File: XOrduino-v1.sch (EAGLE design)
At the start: 56 parts, among them J1 USB MICRO, J2 8x1F-H8.5, J3 8x1F-H8.5, J4 6x1F-H8.5, U1 ATMEGA32U4-XUAU, U10 SLIDER, U3 2.5mm, U4 2.5mm, U5 2.5mm, U6 2.5mm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

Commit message: Attempt to route the board.  90% routed; may need to go to 4 layer board.
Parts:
- removed JP1: 10x1F-H8.5, SmartPrj:PINHD-1X10
- J1: value USB MICRO -> 10x1F-H8.5; device SmartPrj:MYCON2_USB-MINI-B -> SmartPrj:PINHD-1X10
- JP6: value (none) -> Sensor Routing
- L, ON, RX, TX: device led:LED5MM -> led:LED3MM
- S1: value (none) -> RESET
- S2: value 12mm Button -> 6mm Button; device SparkFun:SWITCH-MOMENTARY-212MM -> SparkFun-Electromechanical:TAC_SWITCHPTH
- U10: value SLIDER -> 10k; device SparkFun:SLIDER -> SparkFun-Electromechanical:POT
- renumbered U3 to J5, U4 to J6, U5 to J7, U6 to J8
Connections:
- removed net USBID: J1.ID
- net +5V: now also RN4D.2; no longer RN4C.2
- net A0: now also JP6-1.1; no longer JP6-1.2
- net A1: now also JP6-2.1; no longer JP6-2.2
- net A2: now also JP6-3.1; no longer JP6-3.2
- net A3: now also JP6-4.1; no longer JP6-4.2
- net A4: now also JP6-5.1; no longer JP6-5.2
- net A5: now also JP6-6.1; no longer JP6-6.2
- net AREF: now also J1.8; no longer JP1.8
- net D+: no longer J1.D+
- net D-: no longer J1.D-
- net D2/SDA: now also J1.9; no longer JP1.9
- net D3/SCL: now also J1.10; no longer JP1.10
- net D4: now also JP6-7.1; no longer JP6-7.2
- net GND: now also J1.7, S2.4; no longer J1.SH1, J1.SH2, J1.SH3, J1.SH4, J1.SH5, J1.SH6, JP1.7, S1.3, S2.2
- net IO10*: now also J1.3; no longer JP1.3
- net IO11*: now also J1.4; no longer JP1.4
- net IO12: now also J1.5; no longer JP1.5
- net IO13*: now also J1.6; no longer JP1.6
- net IO8: now also J1.1; no longer JP1.1
- net IO9*: now also J1.2; no longer JP1.2
- net LIGHT: now also JP6-6.2; no longer JP6-6.1
- net N$1: now also RN4B.1; no longer RN4A.1
- net N$2: now also RN4C.1; no longer RN4D.1
- net N$3: now also RN4D.1; no longer RN4C.1
- net N$4: now also RN4A.1; no longer RN4B.1
- net N$6: now also RN4C.2; no longer RN4D.2
- net RA: now also JP6-1.2; no longer JP6-1.1
- net RB: now also JP6-2.2; no longer JP6-2.1
- net RC: now also JP6-3.2; no longer JP6-3.1
- net RD: now also JP6-4.2; no longer JP6-4.1
- net RESET: no longer S1.2
- net SLIDER: now also JP6-7.2; no longer JP6-7.1
- net SOUND: now also JP6-5.2; no longer JP6-5.1
- net UGND: no longer J1.GND
- net XUSB: no longer J1.VBUS
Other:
- moved on the sheet: JP6-1, JP6-2, JP6-3, JP6-4, JP6-5, JP6-6, JP6-7, RN4

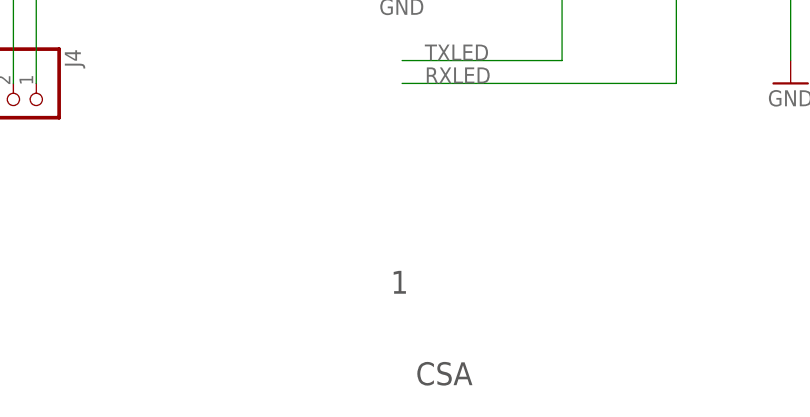
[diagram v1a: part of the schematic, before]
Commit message: XOrduino v2 -- move USB plug up a bit to allow XOstick to fit underneath.
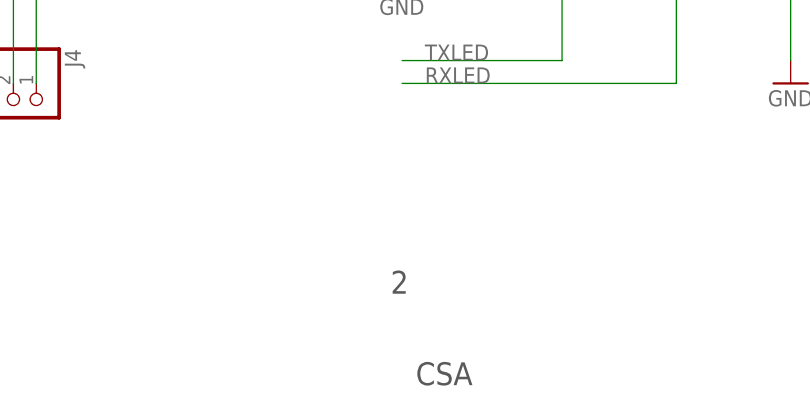
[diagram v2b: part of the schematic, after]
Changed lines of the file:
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@@
 <grid distance="0.1" unitdist="inch" unit="inch" style="lines" multiple="1" display="no" altdistance="0.01" altunitdist="inch" altunit="inch"/>
 <layers>
-<layer number="1" name="Top" color="4" fill="1" visible="yes" active="no"/>
-<layer number="2" name="Route2" color="1" fill="3" visible="yes" active="no"/>
-<layer number="3" name="Route3" color="4" fill="3" visible="yes" active="no"/>
-<layer number="4" name="Route4" color="1" fill="4" visible="yes" active="no"/>
-<layer number="5" name="Route5" color="4" fill="4" visible="yes" active="no"/>
-<layer number="6" name="Route6" color="1" fill="8" visible="yes" active="no"/>
-<layer number="7" name="Route7" color="4" fill="8" visible="yes" active="no"/>
-<layer number="8" name="Route8" color="1" fill="2" visible="yes" active="no"/>
-<layer number="9" name="Route9" color="4" fill="2" visible="yes" active="no"/>
-<layer number="10" name="Route10" color="1" fill="7" visible="yes" active="no"/>
-<layer number="11" name="Route11" color="4" fill="7" visible="yes" active="no"/>
-<layer number="12" name="Route12" color="1" fill="5" visible="yes" active="no"/>
-<layer number="13" name="Route13" color="4" fill="5" visible="yes" active="no"/>
-<layer number="14" name="Route14" color="1" fill="6" visible="yes" active="no"/>
-<layer number="15" name="Route15" color="4" fill="6" visible="yes" active="no"/>
-<layer number="16" name="Bottom" color="1" fill="1" visible="yes" active="no"/>
-<layer number="17" name="Pads" color="2" fill="1" visible="yes" active="no"/>
-<layer number="18" name="Vias" color="14" fill="1" visible="yes" active="no"/>
-<layer number="19" name="Unrouted" color="6" fill="1" visible="yes" active="no"/>
-<layer number="20" name="Dimension" color="15" fill="1" visible="yes" active="no"/>
-<layer number="21" name="tPlace" color="7" fill="1" visible="yes" active="no"/>
-<layer number="22" name="bPlace" color="7" fill="1" visible="yes" active="no"/>
-<layer number="23" name="tOrigins" color="15" fill="1" visible="yes" active="no"/>
-<layer number="24" name="bOrigins" color="15" fill="1" visible="yes" active="no"/>
-<layer number="25" name="tNames" color="7" fill="1" visible="yes" active="no"/>
-<layer number="26" name="bNames" color="7" fill="1" visible="yes" active="no"/>
-<layer number="27" name="tValues" color="7" fill="1" visible="yes" active="no"/>
-<layer number="28" name="bValues" color="7" fill="1" visible="yes" active="no"/>
+<layer number="1" name="Top" color="4" fill="1" visible="no" active="no"/>
+<layer number="2" name="Route2" color="1" fill="3" visible="no" active="no"/>
+<layer number="3" name="Route3" color="4" fill="3" visible="no" active="no"/>
+<layer number="4" name="Route4" color="1" fill="4" visible="no" active="no"/>
+<layer number="5" name="Route5" color="4" fill="4" visible="no" active="no"/>
+<layer number="6" name="Route6" color="1" fill="8" visible="no" active="no"/>
+<layer number="7" name="Route7" color="4" fill="8" visible="no" active="no"/>
+<layer number="8" name="Route8" color="1" fill="2" visible="no" active="no"/>
+<layer number="9" name="Route9" color="4" fill="2" visible="no" active="no"/>
+<layer number="10" name="Route10" color="1" fill="7" visible="no" active="no"/>
+<layer number="11" name="Route11" color="4" fill="7" visible="no" active="no"/>
+<layer number="12" name="Route12" color="1" fill="5" visible="no" active="no"/>
+<layer number="13" name="Route13" color="4" fill="5" visible="no" active="no"/>
+<layer number="14" name="Route14" color="1" fill="6" visible="no" active="no"/>
+<layer number="15" name="Route15" color="4" fill="6" visible="no" active="no"/>
+<layer number="16" name="Bottom" color="1" fill="1" visible="no" active="no"/>
+<layer number="17" name="Pads" color="2" fill="1" visible="no" active="no"/>
+<layer number="18" name="Vias" color="14" fill="1" visible="no" active="no"/>
+<layer number="19" name="Unrouted" color="6" fill="1" visible="no" active="no"/>
+<layer number="20" name="Dimension" color="15" fill="1" visible="no" active="no"/>
+<layer number="21" name="tPlace" color="7" fill="1" visible="no" active="no"/>
+<layer number="22" name="bPlace" color="7" fill="1" visible="no" active="no"/>
+<layer number="23" name="tOrigins" color="15" fill="1" visible="no" active="no"/>
+<layer number="24" name="bOrigins" color="15" fill="1" visible="no" active="no"/>
+<layer number="25" name="tNames" color="7" fill="1" visible="no" active="no"/>
+<layer number="26" name="bNames" color="7" fill="1" visible="no" active="no"/>
+<layer number="27" name="tValues" color="7" fill="1" visible="no" active="no"/>
+<layer number="28" name="bValues" color="7" fill="1" visible="no" active="no"/>
 <layer number="29" name="tStop" color="2" fill="3" visible="no" active="no"/>
 <layer number="30" name="bStop" color="5" fill="6" visible="no" active="no"/>
@@
 <layer number="35" name="tGlue" color="7" fill="4" visible="no" active="no"/>
 <layer number="36" name="bGlue" color="7" fill="5" visible="no" active="no"/>
-<layer number="37" name="tTest" color="7" fill="1" visible="yes" active="no"/>
-<layer number="38" name="bTest" color="7" fill="1" visible="yes" active="no"/>
+<layer number="37" name="tTest" color="7" fill="1" visible="no" active="no"/>
+<layer number="38" name="bTest" color="7" fill="1" visible="no" active="no"/>
 <layer number="39" name="tKeepout" color="4" fill="11" visible="no" active="no"/>
 <layer number="40" name="bKeepout" color="1" fill="11" visible="no" active="no"/>
@@
 <layer number="44" name="Drills" color="7" fill="1" visible="no" active="no"/>
 <layer number="45" name="Holes" color="7" fill="1" visible="no" active="no"/>
-<layer number="46" name="Milling" color="3" fill="1" visible="yes" active="no"/>
-<layer number="47" name="Measures" color="7" fill="1" visible="yes" active="no"/>
-<layer number="48" name="Document" color="7" fill="1" visible="yes" active="no"/>
-<layer number="49" name="Reference" color="13" fill="1" visible="yes" active="no"/>
-<layer number="50" name="dxf" color="12" fill="1" visible="yes" active="no"/>
-<layer number="51" name="tDocu" color="7" fill="1" visible="yes" active="no"/>
-<layer number="52" name="bDocu" color="7" fill="1" visible="yes" active="no"/>
-<layer number="53" name="tGND_GNDA" color="7" fill="1" visible="yes" active="no"/>
-<layer number="54" name="bGND_GNDA" color="7" fill="1" visible="yes" active="no"/>
-<layer number="56" name="wert" color="7" fill="1" visible="yes" active="no"/>
+<layer number="46" name="Milling" color="3" fill="1" visible="no" active="no"/>
+<layer number="47" name="Measures" color="7" fill="1" visible="no" active="no"/>
+<layer number="48" name="Document" color="7" fill="1" visible="no" active="no"/>
+<layer number="49" name="Reference" color="13" fill="1" visible="no" active="no"/>
+<layer number="50" name="dxf" color="12" fill="1" visible="no" active="no"/>
+<layer number="51" name="tDocu" color="7" fill="1" visible="no" active="no"/>
+<layer number="52" name="bDocu" color="7" fill="1" visible="no" active="no"/>
+<layer number="53" name="tGND_GNDA" color="7" fill="1" visible="no" active="no"/>
+<layer number="54" name="bGND_GNDA" color="7" fill="1" visible="no" active="no"/>
+<layer number="56" name="wert" color="7" fill="1" visible="no" active="no"/>
 <layer number="91" name="Nets" color="2" fill="1" visible="yes" active="yes"/>
 <layer number="92" name="Busses" color="1" fill="1" visible="yes" active="yes"/>
@@
 <text x="-120.142" y="-31.496" size="1.27" layer="97">optional</text>
 <text x="169.926" y="43.434" size="1.27" layer="97">optional</text>
-<text x="189.23" y="-58.928" size="2.54" layer="97">1</text>
+<text x="189.23" y="-58.928" size="2.54" layer="97">2</text>
 <text x="192.024" y="-69.088" size="2.54" layer="97">CSA</text>
 <text x="40.64" y="30.48" size="3.81" layer="94" ratio="10" rot="MR0">Scratch Sensor Board</text>
